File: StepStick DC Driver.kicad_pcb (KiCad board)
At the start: 4 copper layers, 15.2 x 20.3 mm, 10 parts, among them IC1 TB67H481FNG, J1 Conn_01x08_Pin, J2 Conn_01x08_Pin

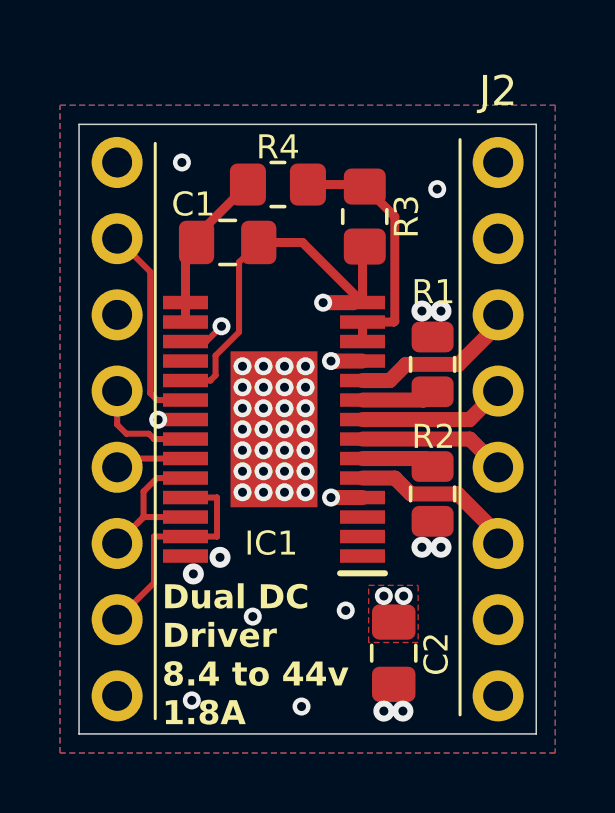
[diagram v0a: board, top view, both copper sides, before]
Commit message: V2 Driver created, Moved V1 to subfolder
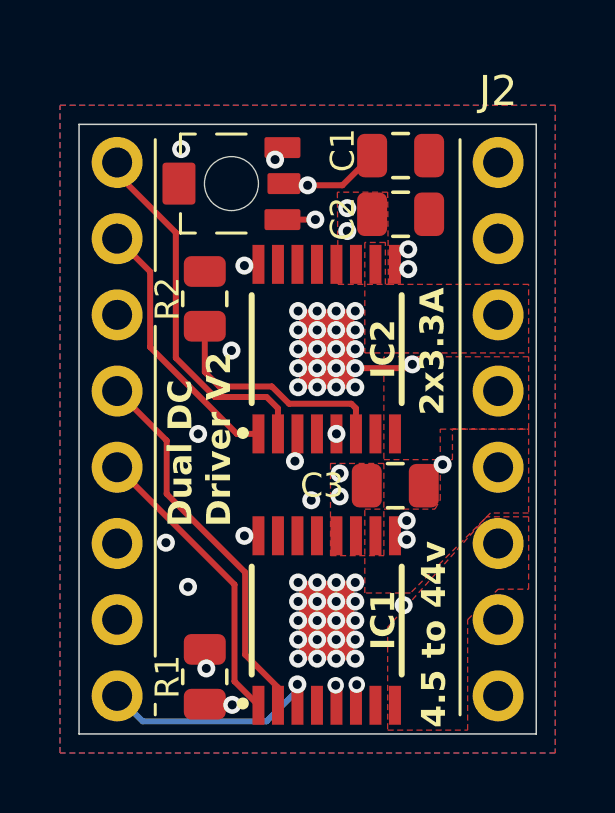
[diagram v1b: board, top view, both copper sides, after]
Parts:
- removed NT1: NetTie_2, NetTie:NetTie-2_SMD_Pad0.5mm
- removed R3: 4.7k, Resistor_SMD:R_0805_2012Metric_Pad1.20x1.40mm_HandSolder
- removed R4: 3k, Resistor_SMD:R_0805_2012Metric_Pad1.20x1.40mm_HandSolder
- added C3: 1u, Capacitor_SMD:C_0805_2012Metric, F.Cu at (132.5, 87.0)
- added IC2: TB67H453FNG, TB67H453FNG:TB67H453FNG, F.Cu at (130.2, 82.4)
- added RV1: R_Potentiometer_Trim 100k, POT_EVM3R:POT_EVM3R, F.Cu at (127.0, 76.9)
- C1, C2: footprint Capacitor_SMD:C_0805_2012Metric_Pad1.18x1.45mm_HandSolder -> Capacitor_SMD:C_0805_2012Metric
- IC1: value TB67H481FNG -> TB67H453FNG; footprint TB67H481FNG:SOP65P640X120-29N -> TB67H453FNG:TB67H453FNG
- R1, R2: value 0R11 -> 1k
- moved C2 14.6 mm to (132.6, 77.9), turned to 180 degrees
- moved R1 12.9 mm to (126.1, 93.3)
- moved R2 10.00 mm to (126.1, 80.7), turned to -90 degrees
- moved IC1 6.61 mm to (130.2, 91.5), turned to 90 degrees
- moved C1 6.45 mm to (132.6, 76.0)
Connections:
- C1 pad 1: +3.3V -> /VREF
- C2 pad 1: /VMOT -> GND
- C2 pad 2: GNDPWR -> /VMOT
- IC1 pad 1: unconnected-(IC1-NC_1-Pad1) -> /MS3
- IC1 pad 10: /OB1 -> /OA2
- IC1 pad 12: Net-(IC1-VREFA) -> unconnected-(IC1-NC_1-Pad12)
- IC1 pad 13: Net-(IC1-VREFA) -> unconnected-(IC1-NC_2-Pad13)
- IC1 pad 14: GND -> unconnected-(IC1-NC_3-Pad14)
- IC1 pad 15: +3.3V -> GND
- IC1 pad 16: +3.3V -> /MS1
- IC1 pad 17: /EN -> GND
- IC1 pad 2: unconnected-(IC1-NC_2-Pad2) -> /RESET
- IC1 pad 3: unconnected-(IC1-NC_3-Pad3) -> /EN
- IC1 pad 4: /VMOT -> unconnected-(IC1-NFAULT-Pad4)
- IC1 pad 5: /OA1 -> /VREF
- IC1 pad 6: /RSA -> Net-(IC1-ISENSE)
- IC1 pad 7: /OA2 -> GND
- IC1 pad 8: /OB2 -> /OA1
- IC1 pad 9: /RSB -> GND
- J2 pad 1: GNDPWR -> GND
- J2 pad 2: unconnected-(J2-Pin_2-Pad2) -> /VCC
- J2 pad 7: GNDPWR -> GND
- R1 pad 1: GNDPWR -> GND
- R1 pad 2: /RSB -> Net-(IC1-ISENSE)
- R2 pad 1: GNDPWR -> GND
- R2 pad 2: /RSA -> Net-(IC2-ISENSE)
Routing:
- net /VREF: track 0.00 -> 26.2 mm, vias 0 -> 3
- net GND: track 12.3 -> 1.96 mm, vias 0 -> 55
- net /RESET: track 3.60 -> 12.7 mm
- net Net-(IC1-VREFA): track 8.57 -> 0.00 mm
- net /VCC: track 0.00 -> 8.48 mm, vias 0 -> 1
- net Net-(IC2-ISENSE): track 0.00 -> 7.83 mm
- net /MS3: track 2.40 -> 9.89 mm
- net /MS2: track 5.39 -> 12.5 mm, vias 0 -> 1
- net Net-(IC1-ISENSE): track 0.00 -> 6.46 mm, vias 0 -> 2
- net /OB1: track 5.62 -> 0.00 mm
- net /OA1: track 5.60 -> 0.00 mm
- net +3.3V: track 5.45 -> 0.00 mm
- net /OB2: track 4.91 -> 0.00 mm
- net /OA2: track 4.91 -> 0.00 mm
- net /EN: track 15.2 -> 18.9 mm, vias 1 -> 2
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- added copper zone on F.Cu, net /OA1
- added copper zone on F.Cu, net /OA2
- added copper zone on F.Cu, net /OB1
- added copper zone on F.Cu, net /OB2
- added copper zone on B.Cu, net GND
- added copper zone on F.Cu, net GND
- added copper zone on In1.Cu, net GND
- added copper zone on In2.Cu, net GND
- removed copper zone on B.Cu, net GNDPWR
- removed copper zone on F.Cu, net GNDPWR
- removed copper zone on In1.Cu, net GNDPWR
- removed copper zone on In2.Cu, net GNDPWR
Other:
- board text added: "2x3.3A"
- board text added: "4.5 to 44v"
- board text added: "Dual DC Driver V2"
- board text added: "MSA"
- board text added: "MSB"
- board text added: "VCC"
- board text added: "Vref(v)= Imax(A)"
- board text removed: "Dual DC Driver 8.4 to 44v 1.8A"
- board text removed: "MS1"
- board text removed: "MS2"
